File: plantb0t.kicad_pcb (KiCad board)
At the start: 2 copper layers, 50 x 50 mm, 60 parts, among them P1 CONN_02X09, P10 CONN_01X01, P11 CONN_01X01, P12 CONN_01X01, P13 CONN_01X01, P2 USB_OTG, P3 CONN_02X03, P4 CONN_01X02, P5 CONN_01X02, P6 CONN_01X02, P7 CONN_01X02, P8 CONN_01X04, P9 CONN_01X04, Q1 BS170, Q2 BS170, SW1 SWITCH_INV, U1 ESP-12, U10 BMP280, U11 74HC(T)4051, U12 LEDx2, U2 CP2102, U3 ZXCL5213V30H5CT-ND, U4 MCP4017 100K, U5 FXL6408, U6 FC6946010R, U7 FC6946010R, U8 MCP6001, U9 PSSI2021SAY

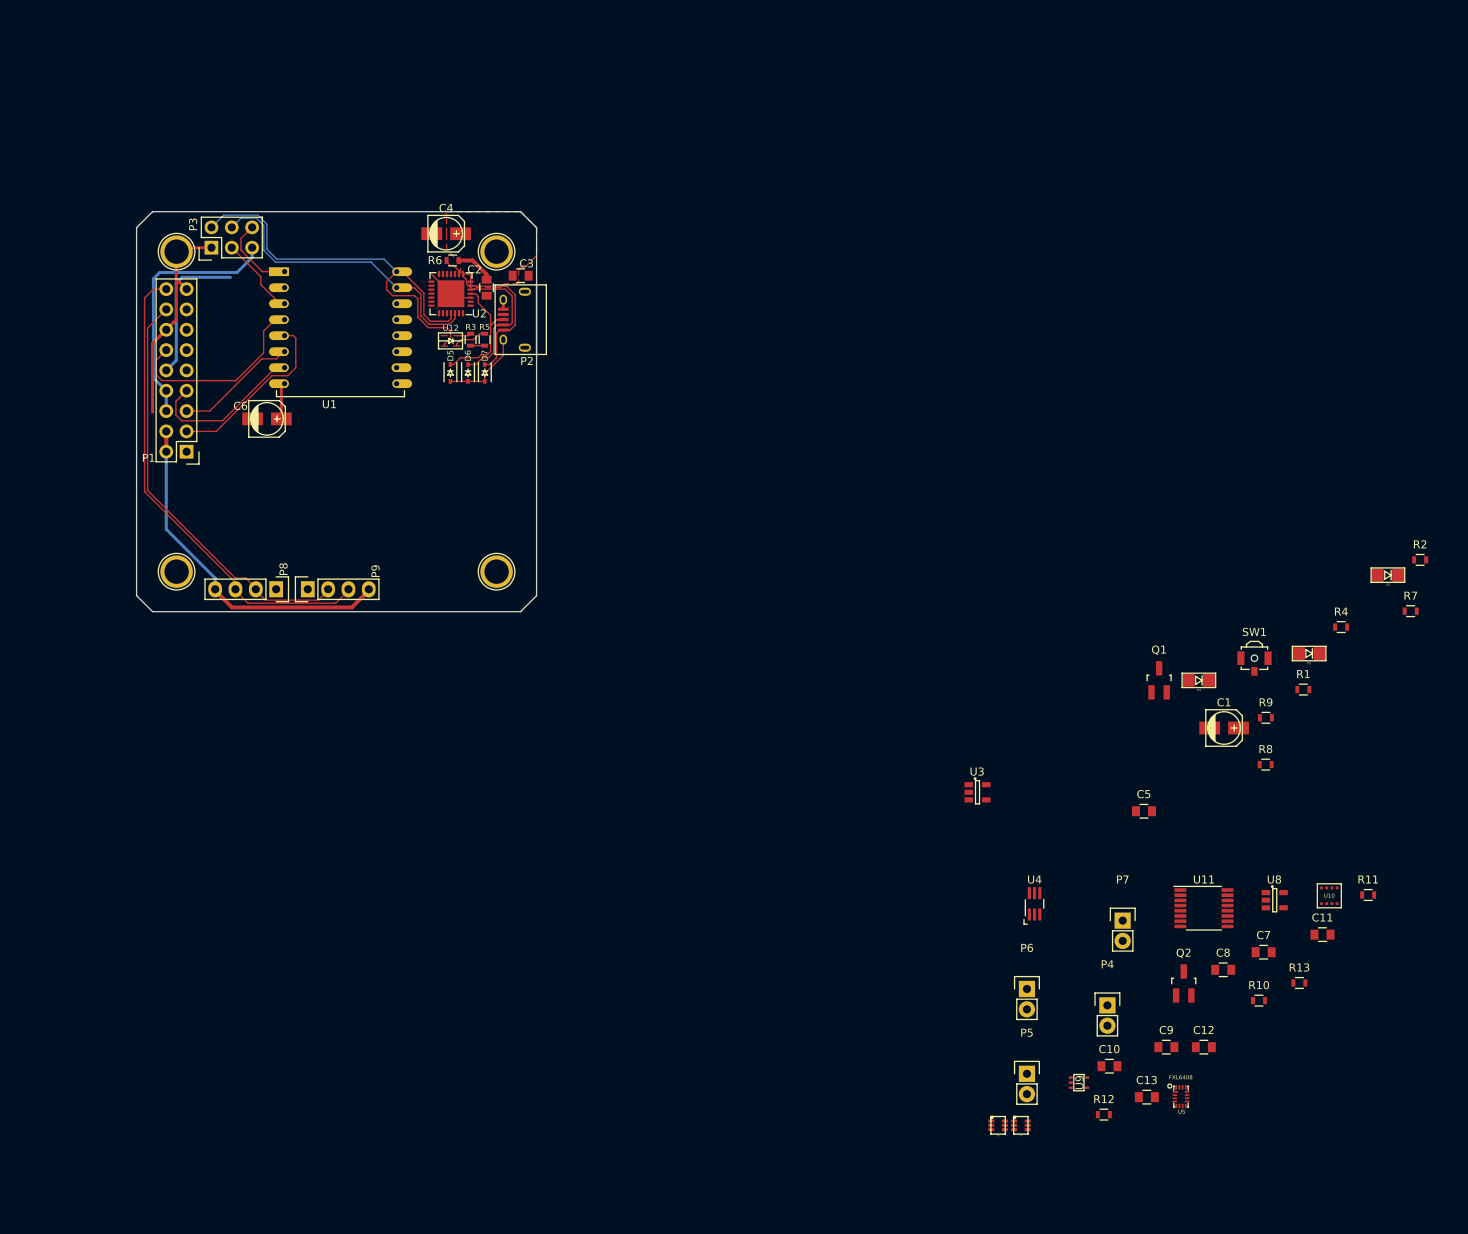
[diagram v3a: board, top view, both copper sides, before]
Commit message: Moving analog section and adding power gating
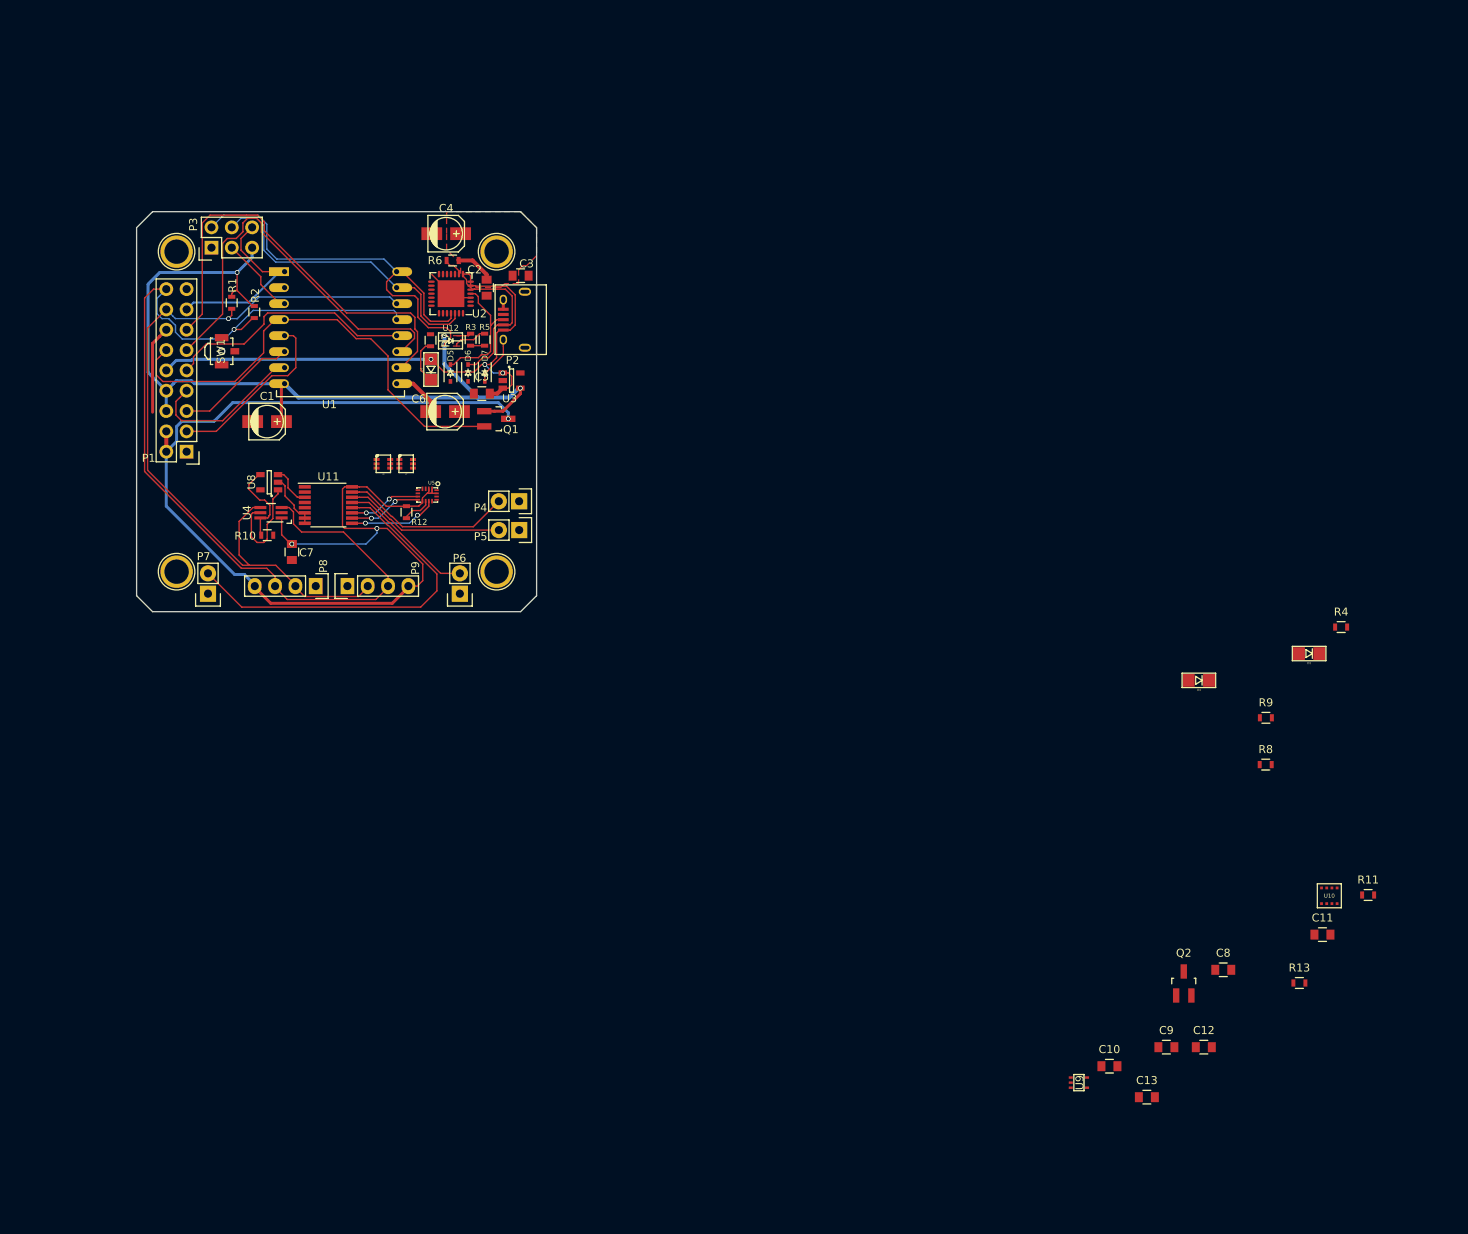
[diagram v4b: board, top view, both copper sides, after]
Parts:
- moved R2 149.0 mm to (79.7, 52.5), turned to 270 degrees
- moved R1 142.4 mm to (76.9, 51.4), turned to 270 degrees
- moved R10 136.9 mm to (81.3, 80.4)
- moved U8 136.1 mm to (81.6, 73.8), turned to 180 degrees
- moved SW1 134.7 mm to (75.6, 57.5), turned to 90 degrees
- moved C7 131.4 mm to (84.4, 82.5), turned to 270 degrees
- moved R7 127.1 mm to (101.7, 56.1), turned to 270 degrees
- moved C1 125.6 mm to (81.3, 66.2)
- moved D3 122.3 mm to (101.8, 59.7), turned to 270 degrees
- moved P7 121.4 mm to (73.9, 87.8), turned to 180 degrees
- moved U5 120.6 mm to (101.3, 75.4), turned to 270 degrees
- moved U11 120.5 mm to (89.0, 76.7)
- moved R12 115.2 mm to (98.7, 77.6), turned to 270 degrees
- moved U6 112.9 mm to (95.8, 71.5)
- moved U7 112.9 mm to (98.7, 71.5)
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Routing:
- net +3V3: track 43.5 -> 145.3 mm, vias 0 -> 3
- net /PERM_3V3: track 36.4 -> 105.1 mm, vias 0 -> 3
- net /I2C_CLOCK: track 60.0 -> 123.3 mm, vias 0 -> 1
- net /GPIO_7: track 0.00 -> 54.9 mm
- net /GPIO_6: track 0.00 -> 51.4 mm
- net /Sensor Mounts/SENSE_D: track 0.00 -> 47.4 mm
- net /I2C_DATA: track 52.7 -> 97.5 mm, vias 0 -> 1
- net /SLEEP_CTRL: track 24.7 -> 57.8 mm
- net /GPIO_5: track 0.00 -> 31.4 mm
- net +5V: track 43.3 -> 74.4 mm, vias 0 -> 3
- net /Sensor Mounts/SENSE_A: track 0.00 -> 21.5 mm
- net /Sensor Mounts/SENSE_B: track 0.00 -> 20.1 mm
- net /Sensor Mounts/SENSE_C: track 0.00 -> 17.2 mm
- net /ESP_RESET: track 9.99 -> 24.2 mm
- net /SENSORS: track 0.00 -> 13.2 mm
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
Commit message: Correcting a wire issue around bosch sensor Finishing basic routing I²C goes through VIAS. Is that an issue?
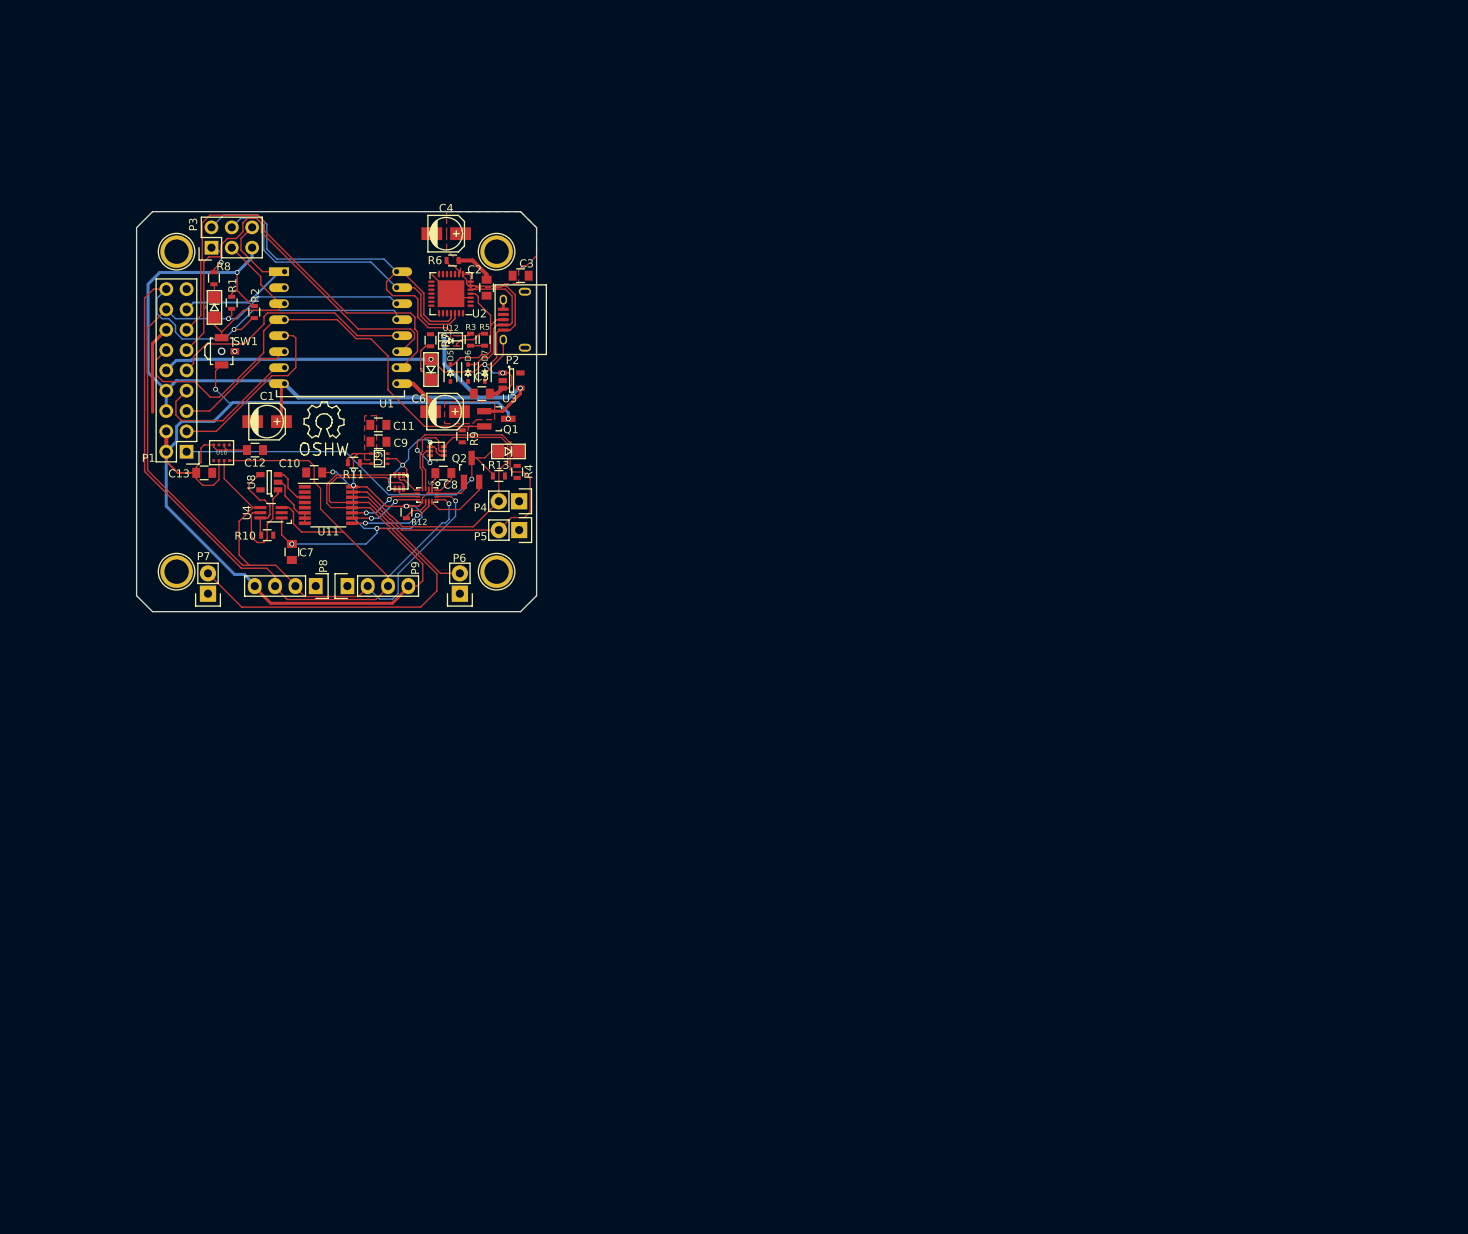
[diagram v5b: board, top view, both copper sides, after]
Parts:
- added REF**: Symbol_OSHW-Logo_SilkScreen, Symbols:Symbol_OSHW-Logo_SilkScreen, F.Cu at (88.4, 66.2)
- moved U10 149.1 mm to (75.6, 70.1), turned to 180 degrees
- moved R8 144.8 mm to (74.7, 48.3), turned to 270 degrees
- moved C13 141.3 mm to (73.5, 72.7)
- moved C12 140.1 mm to (79.8, 69.8)
- moved R11 137.8 mm to (92.2, 71.4)
- moved C11 134.1 mm to (95.2, 66.7), turned to 180 degrees
- moved D4 131.6 mm to (74.7, 52.0), turned to 90 degrees
- moved C9 124.2 mm to (95.2, 68.8), turned to 180 degrees
- moved C10 124.1 mm to (87.2, 72.6), turned to 180 degrees
- moved R13 118.4 mm to (110.3, 73.0)
- moved U9 117.2 mm to (95.3, 70.9), turned to 180 degrees
- moved C8 115.6 mm to (103.3, 72.7)
- moved Q2 109.8 mm to (106.9, 72.3)
- moved R9 106.4 mm to (105.7, 68.1), turned to 270 degrees
- moved R4 104.8 mm to (112.6, 72.5), turned to 90 degrees
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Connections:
- C12 pad 1: GND -> +3V3
- C13 pad 1: Net-(C13-Pad1) -> +3V3
- U10 pad 8: Net-(C13-Pad1) -> +3V3
- U6 pad 1: /Sensor Mounts/SENSE_A -> /Sensor Mounts/SENSOR_PWR
- U6 pad 3: /Sensor Mounts/SENSOR_PWR -> /Sensor Mounts/SENSE_B
- U6 pad 4: /Sensor Mounts/SENSOR_B -> /Sensor Mounts/SENSOR_PWR
- U6 pad 6: /Sensor Mounts/SENSE_B -> /Sensor Mounts/SENSE_A
- U7 pad 1: /Sensor Mounts/SENSE_C -> /Sensor Mounts/SENSOR_PWR
- U7 pad 3: /Sensor Mounts/SENSOR_PWR -> /Sensor Mounts/SENSE_D
- U7 pad 4: /Sensor Mounts/SENSOR_D -> /Sensor Mounts/SENSOR_PWR
- U7 pad 6: /Sensor Mounts/SENSE_D -> /Sensor Mounts/SENSE_C
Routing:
- net +3V3: track 145.3 -> 199.7 mm, vias 3 -> 8
- net /GPIO_1: track 0.00 -> 48.2 mm, vias 0 -> 1
- net /I2C_CLOCK: track 123.3 -> 159.4 mm, vias 1 -> 2
- net /Sensor Mounts/SENSE_B: track 20.1 -> 51.9 mm, vias 0 -> 2
- net /I2C_DATA: track 97.5 -> 126.8 mm, vias 1 -> 2
- net /Sensor Mounts/SENSOR_PWR: track 0.00 -> 16.9 mm, vias 0 -> 3
- net /Sensor Mounts/SENSE_A: track 21.5 -> 37.9 mm
- net /Sensor Mounts/SENSE_C: track 17.2 -> 32.6 mm
- net /Sensor Mounts/SENSE_D: track 47.4 -> 62.1 mm
- net /CH_PD: track 10.1 -> 22.3 mm
- net /Sensor Mounts/SENABLE_B: track 0.00 -> 10.4 mm
- net /Sensor Mounts/GPIO_TRIG: track 0.00 -> 8.84 mm
- net /Sensor Mounts/SENABLE_A: track 0.00 -> 5.53 mm
- net GND: track 46.1 -> 50.4 mm, vias 0 -> 2
- net /Sensor Mounts/SENABLE_C: track 0.00 -> 3.40 mm
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- added copper zone on F.Cu, net +3V3
- added copper zone on F.Cu, net /PERM_3V3
